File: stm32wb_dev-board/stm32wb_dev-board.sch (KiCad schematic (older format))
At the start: 1 part

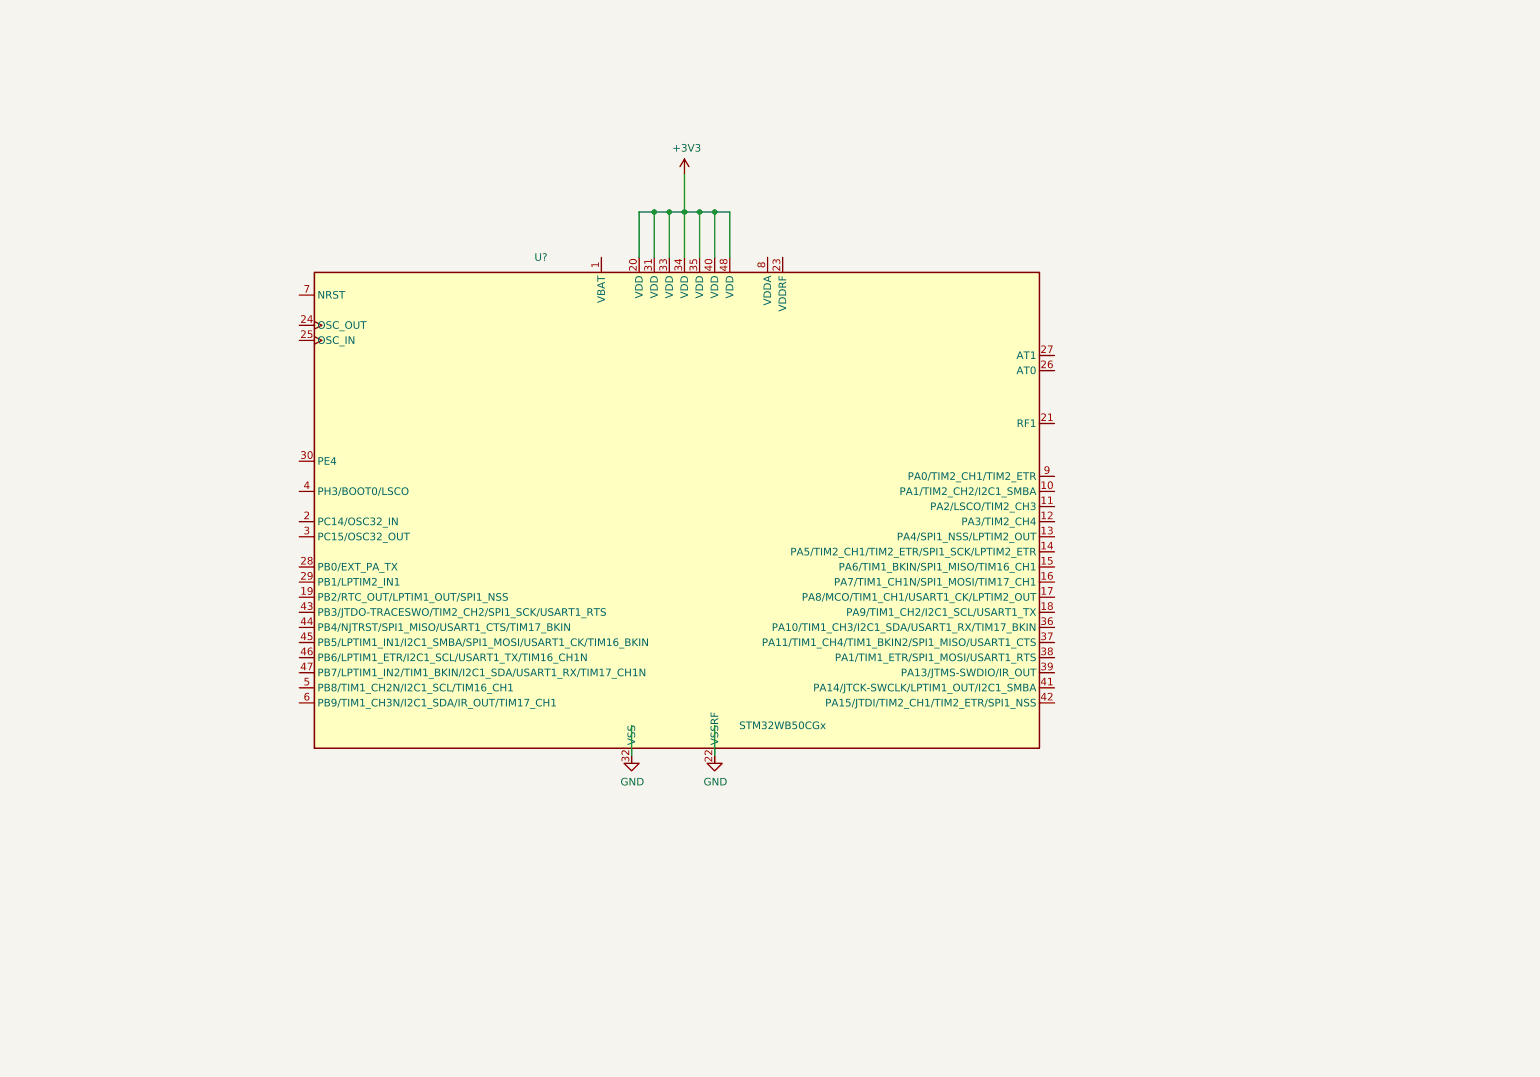
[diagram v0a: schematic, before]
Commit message: Added: crystals, supplier capacitors, connectors
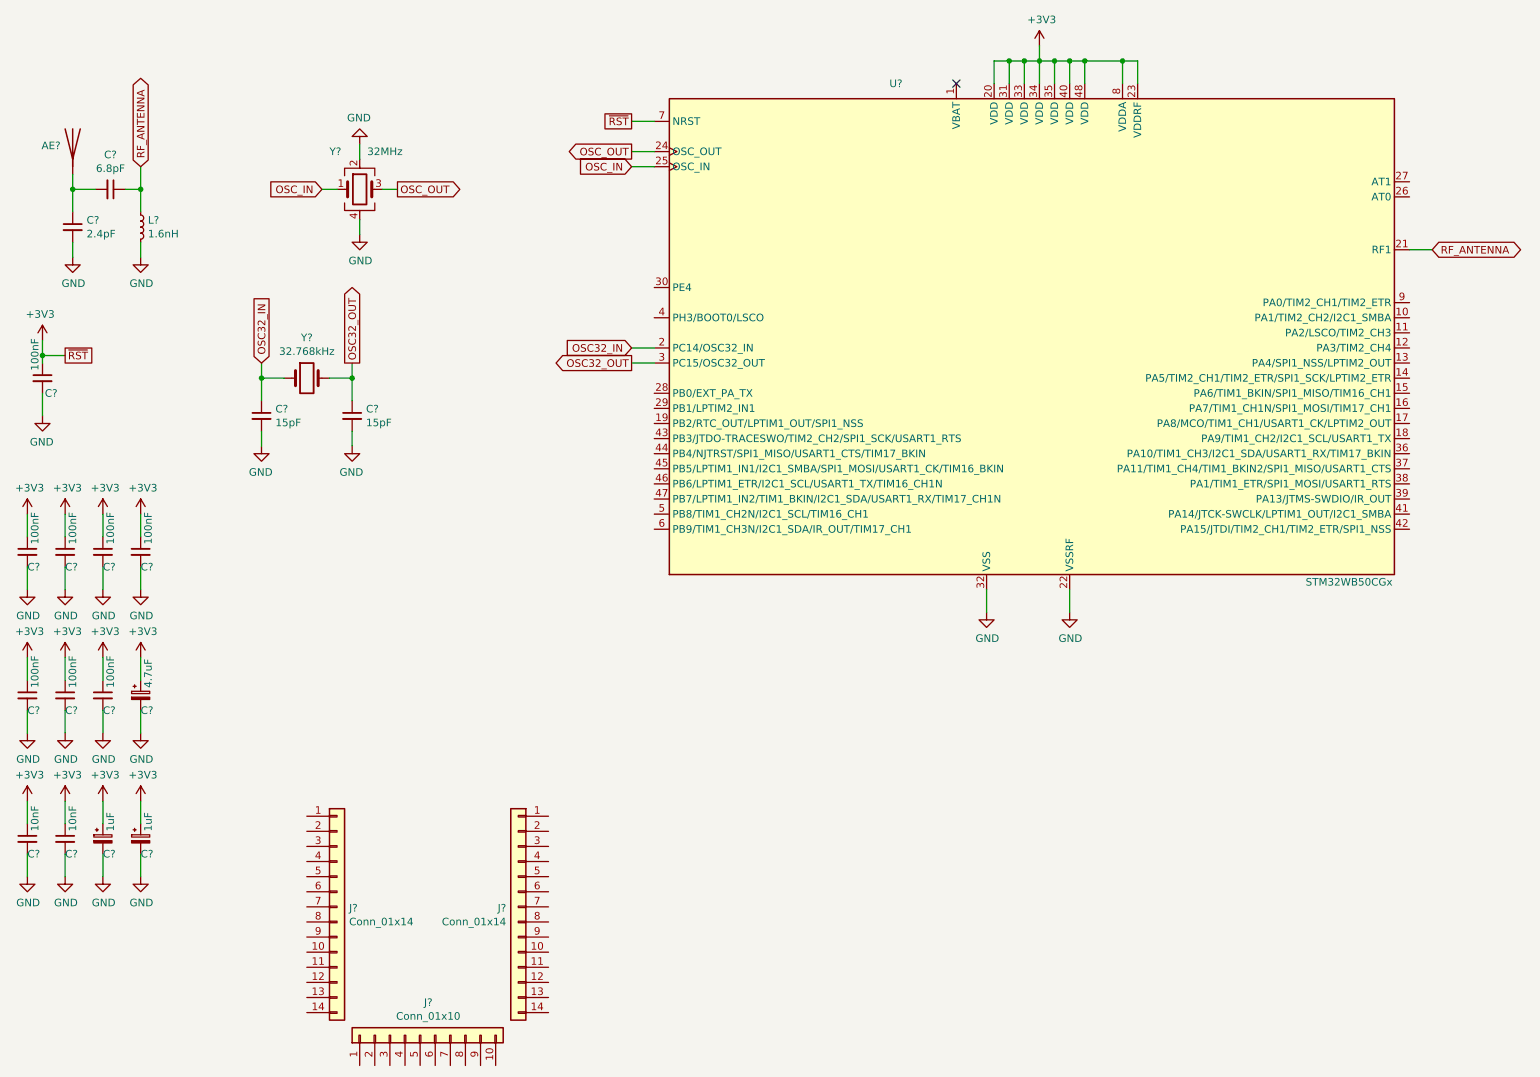
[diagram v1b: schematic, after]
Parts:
- added AE?: Antenna, symbol Device:Antenna
- added C? (x8): 100nF, symbol Device:C_Small
- added C?: 4.7uF, symbol Device:CP_Small
- added C? (x2): 10nF, symbol Device:C_Small
- added C? (x2): 1uF, symbol Device:CP_Small
- added C?: 2.4pF, symbol Device:C_Small
- added C?: 6.8pF, symbol Device:C_Small
- added C? (x2): 15pF, symbol Device:C_Small
- added J? (x2): Conn_01x14, symbol Connector_Generic:Conn_01x14
- added J?: Conn_01x10, symbol Connector_Generic:Conn_01x10
- added L?: 1.6nH, symbol Device:L_Small
- added Y?: 32MHz, symbol Device:Crystal_GND24
- added Y?: 32.768kHz, symbol Device:Crystal
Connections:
- net labels added: OSC32_IN, OSC32_OUT, OSC_IN, OSC_OUT, RF_ANTENNA, ~RST
- wire segments 16 -> 74
- no-connect marks 0 -> 1
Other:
- moved on the sheet: U?
